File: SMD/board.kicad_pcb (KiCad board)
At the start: 2 copper layers, 30 x 60 mm, 28 parts, among them J1 9V Battery, J2 Barrel_Jack_Switch, J3 USB_B, J4 1, J5 2, J6 Conn_02x04_Odd_Even, SW1 SW_DIP_x04, U1 LM317_3PinPackage, U2 AMS1117-5.0, U3 AMS1117-3.3

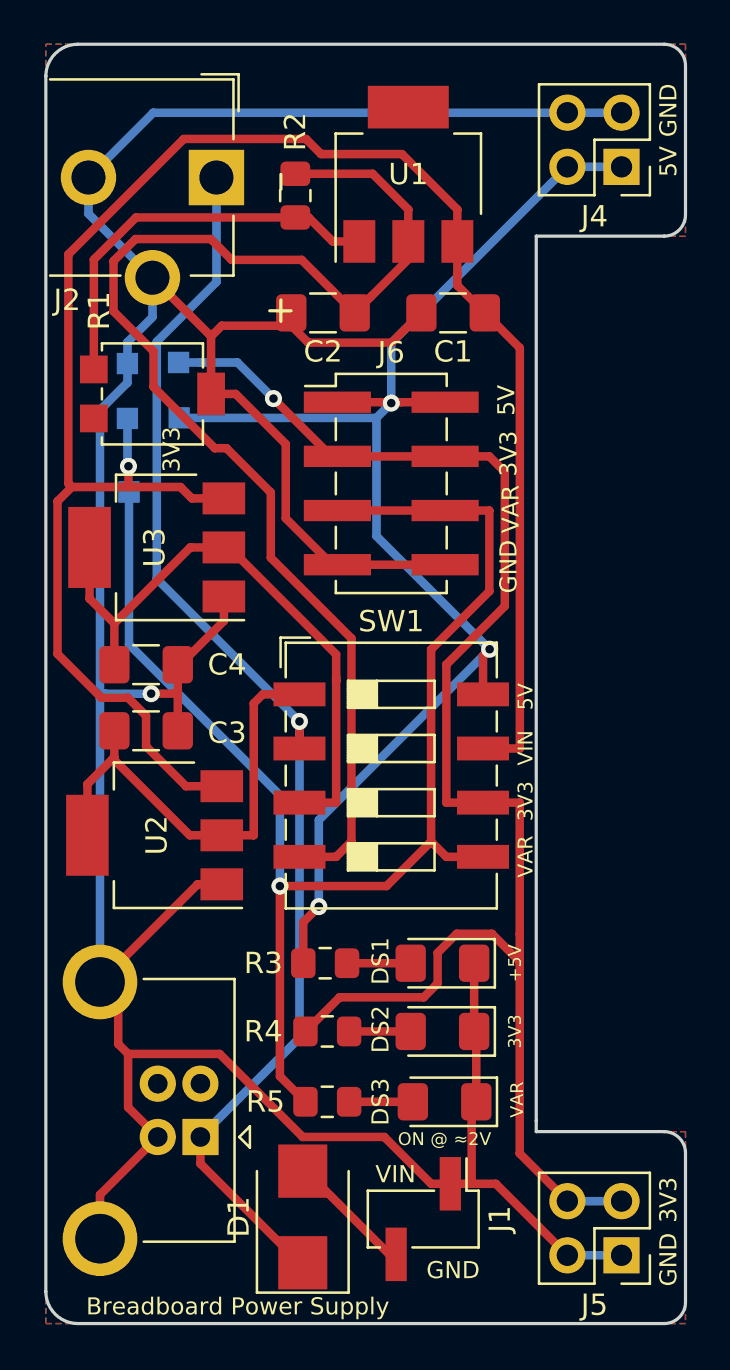
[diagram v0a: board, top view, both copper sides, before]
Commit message: SMD Kicad 10
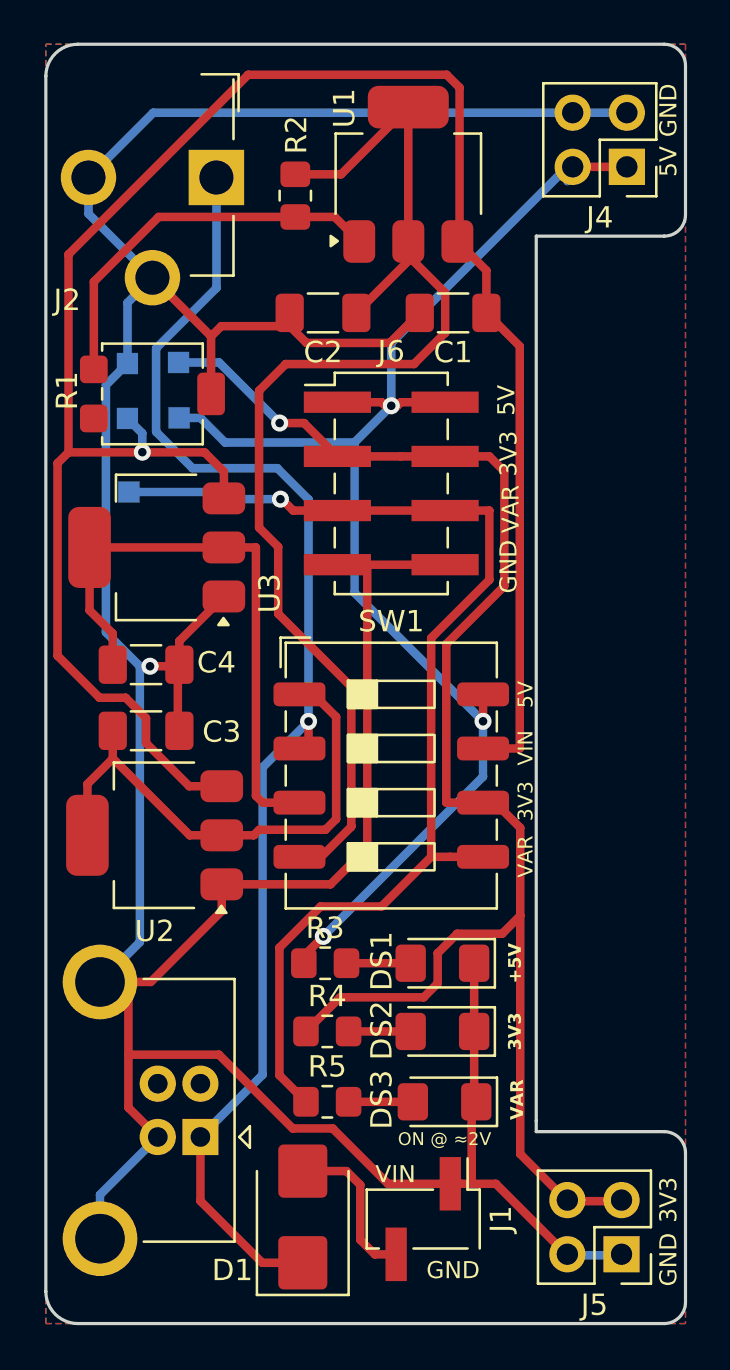
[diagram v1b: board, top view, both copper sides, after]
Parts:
- C1, C2, C3, C4: footprint Capacitor_SMD:C_1206_3216Metric_Pad1.42x1.75mm_HandSolder -> Capacitor_SMD:C_1206_3216Metric_Pad1.33x1.80mm_HandSolder
- J2: footprint Breadboard_Power_Supply:BarrelJack_CUI_PJ-102AH_Horizontal -> Board:BarrelJack_CUI_PJ-102AH_Horizontal
- J3: footprint Breadboard_Power_Supply:USB_B_OST_USB-B1HSxx_Horizontal -> Board:USB_B_OST_USB-B1HSxx_Horizontal
- R2, R3, R5: footprint Resistor_SMD:R_0805_2012Metric_Pad1.15x1.40mm_HandSolder -> Resistor_SMD:R_0805_2012Metric_Pad1.20x1.40mm_HandSolder
- R4: value 1.5k -> 1k; footprint Resistor_SMD:R_0805_2012Metric_Pad1.15x1.40mm_HandSolder -> Resistor_SMD:R_0805_2012Metric_Pad1.20x1.40mm_HandSolder
- U1: value LM317_3PinPackage -> LM317; footprint Package_TO_SOT_SMD:SOT-223 -> Package_TO_SOT_SMD:SOT-223-3_TabPin2
- moved J4 0.25 mm to (159.8, 65.2)
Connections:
- net +3V3 renamed +3.3V
- net /3.3V_OUT renamed /3.3V
- net /5V_OUT renamed /5V
- net /VAR_VLG renamed /V
- net /VAR_VLG_OUT renamed /VOUT
- J3 pad 2: (no net) -> unconnected-(J3-D--Pad2)
- J3 pad 3: (no net) -> unconnected-(J3-D+-Pad3)
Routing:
- net /V: track 66.5 -> 53.7 mm
- net GND: track 171.7 -> 180.1 mm
- net /VIN: track 90.9 -> 96.8 mm
- net /VOUT: track 60.0 -> 56.6 mm
- net VDC: track 60.7 -> 64.0 mm
- net /5V: track 22.0 -> 24.6 mm
- net Net-(D1-A): track 6.09 -> 7.51 mm
- net /3.3V: track 28.9 -> 27.8 mm
- net Net-(U1-ADJ): track 18.9 -> 18.3 mm
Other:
- rule pad_to_mask_clearance: 0.2 -> 0.05
- board text added: "V"
